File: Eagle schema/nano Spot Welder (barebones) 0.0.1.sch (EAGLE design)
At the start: 37 parts, among them Q1 BC548, Q3 BD137, T1 BTA 41 / 600V, U1 NANO, U2 DISPLAY-NOKIA-5110, U3 DS18B20, X3 ~230V, X4 Mikro trafó

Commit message: - eagle schemas
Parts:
- removed U1: NANO, Arduino-clone:NANO
- added C2, C3: 33p, rcl:C-EU025-024X044
- added C4, C5: 100n, rcl:C-EU025-024X044
- added C6: 220u, resistor:CPOL-EUE5-4
- added D2: 1N4148, diode:1N4148DO35-10
- added IC1: 7805T, linear:7805T
- added IC2: 78L33, linear:7805L
- added J1: AVR ISP CONN, SparkFun-Connectors:CONN_03X2SHROUD
- added R6: 1k, resistor:R-EU_0204/7
- added U4: 328P, SparkFun-IC-Microcontroller:ATMEGA328P_PDIP
- added Y1: 16MHz, SparkFun-Clocks:CRYSTAL-16MHZPTH-HC49US
- added ~TÁP: ~9V, con-ptr500:AK300/2
- B1: value (none) -> 1W01M
- R5: value 56kk -> 4k7
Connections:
- removed net +5V: U1.5.5V
- new net N$10: C3.2, U4.PB7(XTAL2/TOSC2), Y1.1
- new net N$11: B1.+, D2.A, R5.1
- new net N$8: C4.2, U4.AREF
- new net N$9: C2.2, U4.PB6(XTAL1/TOSC1), Y1.2
- new net RST: J1.5, R6.2, U4.PC6(/RESET)
- new net VCC1: B1.AC1, ~TÁP-2.KL
- net +3.3V: now also IC2.VO; no longer U1.3.3V
- net A0: now also U4.PC0(ADC0); no longer U1.A0
- net A1: now also U4.PC1(ADC1); no longer U1.A1
- net A2: now also U4.PC2(ADC2); no longer U1.A2
- net A3: now also U4.PC3(ADC3); no longer U1.A3
- net D10: now also U4.PB2(SS/OC1B); no longer U1.D10
- net D11: now also J1.4, U4.PB3(MOSI/OC2); no longer U1.D11
- net D12: now also J1.1, U4.PB4(MISO); no longer U1.D12
- net D13: now also J1.3, U4.PB5(SCK); no longer U1.D13
- net D2: now also U4.PD2(INT0); no longer U1.D2
- net D3: now also U4.PD3(INT1); no longer U1.D3
- net D4: now also U4.PD4(XCK/T0); no longer U1.D4
- net D5: now also U4.PD5(T1); no longer U1.D5
- net D6: now also U4.PD6(AIN0); no longer U1.D6
- net D7: now also U4.PD7(AIN1); no longer U1.D7
- net D8: now also U4.PB0(ICP); no longer U1.D8
- net D9: now also U4.PB1(OC1A); no longer U1.D9
- net GND: now also C2.1, C3.1, C4.1, C5.1, C6.-, IC1.GND, IC2.GND, J1.6, U4.GND@1, U4.GND@2; no longer U1.GND
- net N$25: no longer B1.AC1
- net N$3: now also R5.2; no longer B1.+
- net N$33: no longer R5.2
- net N$7: now also ~TÁP-1.KL; no longer R5.1
- net VCC: now also C5.2, C6.+, D2.C, IC1.VI, IC1.VO, IC2.VI, J1.2, R6.1, U4.AVCC, U4.VCC
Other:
- note added: "+"
- note added: "Arduino Nano MOT vezérlő (barebones)"
- note added: "GND"
- note added: "MISO"
- note added: "MOSI"
- note added: "RST"
- note added: "SCK"
- note removed: "Arduino Nano MOT vezérlő"
- moved on the sheet: B1, OK1, R2, R3, R5

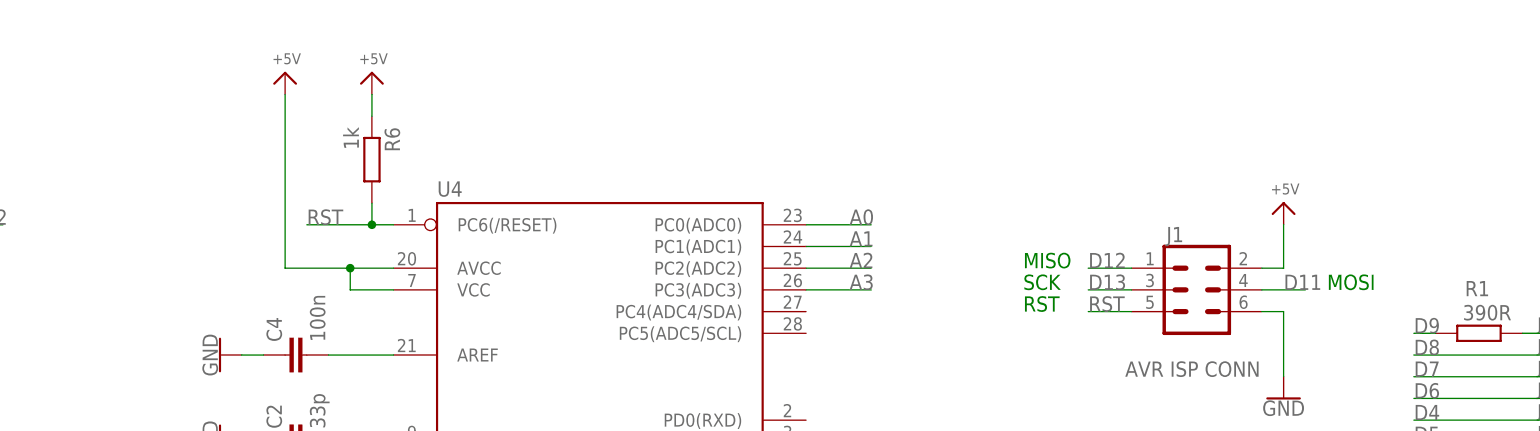
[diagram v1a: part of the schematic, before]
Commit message: - LCD szintillesztő ellenállások - LCD bias & Contrast
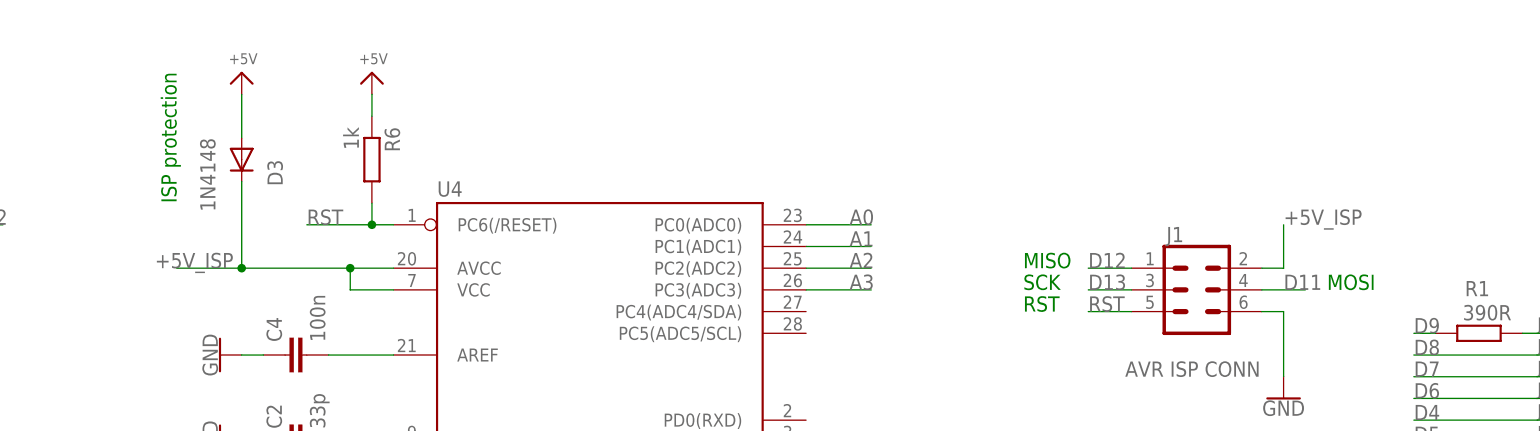
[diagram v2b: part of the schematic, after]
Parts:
- added D3: 1N4148, diode:1N4148DO35-10
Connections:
- new net +5V_ISP: D3.C, J1.2, U4.AVCC, U4.VCC
- net VCC: now also D3.A; no longer J1.2, U4.AVCC, U4.VCC
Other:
- note added: "ISP protection"
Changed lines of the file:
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@@
 <part name="GND15" library="SparkFun-PowerSymbols" library_urn="urn:adsk.eagle:library:530" deviceset="GND" device=""/>
 <part name="R6" library="resistor" library_urn="urn:adsk.eagle:library:348" deviceset="R-EU_" device="0204/7" package3d_urn="urn:adsk.eagle:package:25945/1" value="1k"/>
-<part name="P+5" library="audio amplifier example" library_urn="urn:adsk.eagle:library:970892" deviceset="VCC" device="" value="+5V"/>
 <part name="IC1" library="linear" library_urn="urn:adsk.eagle:library:262" deviceset="78*" device="T" package3d_urn="urn:adsk.eagle:package:16414/1" technology="05"/>
 <part name="IC2" library="linear" library_urn="urn:adsk.eagle:library:262" deviceset="78*" device="L" package3d_urn="urn:adsk.eagle:package:16416/2" technology="05" value="78L33"/>
 <part name="J1" library="SparkFun-Connectors" library_urn="urn:adsk.eagle:library:513" deviceset="CONN_03X2" device="SHROUD" package3d_urn="urn:adsk.eagle:package:38264/1" value="AVR ISP CONN"/>
-<part name="P+8" library="audio amplifier example" library_urn="urn:adsk.eagle:library:970892" deviceset="VCC" device="" value="+5V"/>
 <part name="GND5" library="SparkFun-PowerSymbols" library_urn="urn:adsk.eagle:library:530" deviceset="GND" device=""/>
 <part name="P+9" library="audio amplifier example" library_urn="urn:adsk.eagle:library:970892" deviceset="VCC" device="" value="+5V"/>
@@
 <part name="R5" library="resistor" library_urn="urn:adsk.eagle:library:348" deviceset="R-EU_" device="0204/7" package3d_urn="urn:adsk.eagle:package:25945/1" value="4k7"/>
 <part name="~TÁP" library="con-ptr500" library_urn="urn:adsk.eagle:library:181" deviceset="AK300/2" device="" package3d_urn="urn:adsk.eagle:package:9881/1" value="~9V"/>
+<part name="D3" library="diode" library_urn="urn:adsk.eagle:library:210" deviceset="1N4148" device="DO35-10" package3d_urn="urn:adsk.eagle:package:43344/2" value="1N4148"/>
+<part name="P+5" library="audio amplifier example" library_urn="urn:adsk.eagle:library:970892" deviceset="VCC" device="" value="+5V"/>
 </parts>
 <sheets>
@@
 <text x="25.4" y="121.92" size="1.778" layer="91">SCK</text>
 <text x="25.4" y="119.38" size="1.778" layer="91">RST</text>
+<text x="-73.66" y="132.08" size="1.778" layer="91" rot="R90">
+ISP protection </text>
 </plain>
 <instances>
@@
 <attribute name="VALUE" x="-54.102" y="140.97" size="1.778" layer="96" rot="R270"/>
 </instance>
-<instance part="P+5" gate="VCC" x="-60.96" y="147.32"/>
 <instance part="IC1" gate="A1" x="-152.4" y="12.7"/>
 <instance part="IC2" gate="A1" x="-121.92" y="12.7"/>
@@
 <attribute name="VALUE" x="37.338" y="113.538" size="1.778" layer="96" font="vector" align="top-left"/>
 </instance>
-<instance part="P+8" gate="VCC" x="55.88" y="132.08"/>
 <instance part="GND5" gate="1" x="55.88" y="109.22"/>
 <instance part="P+9" gate="VCC" x="-50.8" y="147.32"/>
@@
 <attribute name="VALUE" x="-156.21" y="72.263" size="1.778" layer="96" rot="MR180"/>
 </instance>
+<instance part="D3" gate="G$1" x="-66.04" y="137.16" smashed="yes" rot="R270">
+<attribute name="NAME" x="-63.0174" y="137.16" size="1.778" layer="95" rot="R270"/>
+<attribute name="VALUE" x="-70.8914" y="139.7" size="1.778" layer="96" rot="R270"/>
+</instance>
+<instance part="P+5" gate="VCC" x="-66.04" y="147.32"/>
 </instances>
 <busses>
@@
 </segment>
 <segment>
-<pinref part="J1" gate="G$1" pin="2"/>
-<wire x1="53.34" y1="124.46" x2="55.88" y2="124.46" width="0.1524" layer="91"/>
-<pinref part="P+8" gate="VCC" pin="VCC"/>
-<wire x1="55.88" y1="124.46" x2="55.88" y2="129.54" width="0.1524" layer="91"/>
-</segment>
-<segment>
-<pinref part="U4" gate="G$1" pin="VCC"/>
-<wire x1="-53.34" y1="121.92" x2="-48.26" y2="121.92" width="0.1524" layer="91"/>
-<pinref part="U4" gate="G$1" pin="AVCC"/>
-<wire x1="-48.26" y1="124.46" x2="-53.34" y2="124.46" width="0.1524" layer="91"/>
-<wire x1="-53.34" y1="124.46" x2="-53.34" y2="121.92" width="0.1524" layer="91"/>
-<wire x1="-53.34" y1="124.46" x2="-60.96" y2="124.46" width="0.1524" layer="91"/>
-<junction x="-53.34" y="124.46"/>
-<pinref part="P+5" gate="VCC" pin="VCC"/>
-<wire x1="-60.96" y1="124.46" x2="-60.96" y2="144.78" width="0.1524" layer="91"/>
-</segment>
-<segment>
 <pinref part="R6" gate="G$1" pin="1"/>
 <pinref part="P+9" gate="VCC" pin="VCC"/>
@@
 <wire x1="-165.1" y1="12.7" x2="-165.1" y2="27.94" width="0.1524" layer="91"/>
 </segment>
+<segment>
+<pinref part="D3" gate="G$1" pin="A"/>
+<pinref part="P+5" gate="VCC" pin="VCC"/>
+<wire x1="-66.04" y1="139.7" x2="-66.04" y2="144.78" width="0.1524" layer="91"/>
+</segment>
 </net>
 <net name="A2" class="0">
@@
 </segment>
 </net>
+<net name="+5V_ISP" class="0">
+<segment>
+<pinref part="U4" gate="G$1" pin="VCC"/>
+<wire x1="-53.34" y1="121.92" x2="-48.26" y2="121.92" width="0.1524" layer="91"/>
+<pinref part="U4" gate="G$1" pin="AVCC"/>
+<wire x1="-48.26" y1="124.46" x2="-53.34" y2="124.46" width="0.1524" layer="91"/>
+<wire x1="-53.34" y1="124.46" x2="-53.34" y2="121.92" width="0.1524" layer="91"/>
+<wire x1="-53.34" y1="124.46" x2="-66.04" y2="124.46" width="0.1524" layer="91"/>
+<junction x="-53.34" y="124.46"/>
+<pinref part="D3" gate="G$1" pin="C"/>
+<wire x1="-66.04" y1="124.46" x2="-66.04" y2="134.62" width="0.1524" layer="91"/>
+<wire x1="-66.04" y1="124.46" x2="-73.66" y2="124.46" width="0.1524" layer="91"/>
+<junction x="-66.04" y="124.46"/>
+<label x="-76.2" y="124.46" size="1.778" layer="95"/>
+</segment>
+<segment>
+<pinref part="J1" gate="G$1" pin="2"/>
+<wire x1="53.34" y1="124.46" x2="55.88" y2="124.46" width="0.1524" layer="91"/>
+<wire x1="55.88" y1="124.46" x2="55.88" y2="129.54" width="0.1524" layer="91"/>
+<label x="55.88" y="129.54" size="1.778" layer="95"/>
+</segment>
+</net>
 </nets>
 </sheet>
@@
 </drawing>
 <compatibility>
+<note version="6.3" minversion="6.2.2" severity="warning">
+Since Version 6.2.2 text objects can contain more than one line,
+which will not be processed correctly with this version.
+</note>
 <note version="8.2" severity="warning">
 Since Version 8.2, EAGLE supports online libraries. The ids

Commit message: - rajzok
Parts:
- removed C4: 100n, rcl:C-EU025-024X044
- removed D3: 1N4148, diode:1N4148DO35-10
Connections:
- removed net N$8: C4.2, U4.AREF
- net +5V_ISP: now also U4.AREF; no longer D3.C
- net GND: no longer C4.1
- net VCC: no longer D3.A
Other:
- note removed: "ISP protection"
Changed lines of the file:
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@@
 <part name="GND13" library="SparkFun-PowerSymbols" library_urn="urn:adsk.eagle:library:530" deviceset="GND" device=""/>
 <part name="GND14" library="SparkFun-PowerSymbols" library_urn="urn:adsk.eagle:library:530" deviceset="GND" device=""/>
-<part name="C4" library="rcl" library_urn="urn:adsk.eagle:library:334" deviceset="C-EU" device="025-024X044" package3d_urn="urn:adsk.eagle:package:23630/1" value="100n"/>
-<part name="GND15" library="SparkFun-PowerSymbols" library_urn="urn:adsk.eagle:library:530" deviceset="GND" device=""/>
 <part name="R6" library="resistor" library_urn="urn:adsk.eagle:library:348" deviceset="R-EU_" device="0204/7" package3d_urn="urn:adsk.eagle:package:25945/1" value="1k"/>
 <part name="IC1" library="linear" library_urn="urn:adsk.eagle:library:262" deviceset="78*" device="T" package3d_urn="urn:adsk.eagle:package:16414/1" technology="05"/>
@@
 <part name="R5" library="resistor" library_urn="urn:adsk.eagle:library:348" deviceset="R-EU_" device="0204/7" package3d_urn="urn:adsk.eagle:package:25945/1" value="4k7"/>
 <part name="~TÁP" library="con-ptr500" library_urn="urn:adsk.eagle:library:181" deviceset="AK300/2" device="" package3d_urn="urn:adsk.eagle:package:9881/1" value="~9V"/>
-<part name="D3" library="diode" library_urn="urn:adsk.eagle:library:210" deviceset="1N4148" device="DO35-10" package3d_urn="urn:adsk.eagle:package:43344/2" value="1N4148"/>
 <part name="P+5" library="audio amplifier example" library_urn="urn:adsk.eagle:library:970892" deviceset="VCC" device="" value="+5V"/>
 </parts>
@@
 <text x="25.4" y="121.92" size="1.778" layer="91">SCK</text>
 <text x="25.4" y="119.38" size="1.778" layer="91">RST</text>
-<text x="-73.66" y="132.08" size="1.778" layer="91" rot="R90">
-ISP protection </text>
 </plain>
 <instances>
@@
 <instance part="GND13" gate="1" x="-68.58" y="99.06" rot="R270"/>
 <instance part="GND14" gate="1" x="-53.34" y="68.58"/>
-<instance part="C4" gate="G$1" x="-60.96" y="114.3" rot="R90"/>
-<instance part="GND15" gate="1" x="-68.58" y="114.3" rot="R270"/>
 <instance part="R6" gate="G$1" x="-50.8" y="137.16" smashed="yes" rot="R270">
 <attribute name="NAME" x="-49.3014" y="140.97" size="1.778" layer="95" rot="R270"/>
@@
 <attribute name="NAME" x="-161.29" y="67.691" size="1.778" layer="95" rot="MR0"/>
 <attribute name="VALUE" x="-156.21" y="72.263" size="1.778" layer="96" rot="MR180"/>
-</instance>
-<instance part="D3" gate="G$1" x="-66.04" y="137.16" smashed="yes" rot="R270">
-<attribute name="NAME" x="-63.0174" y="137.16" size="1.778" layer="95" rot="R270"/>
-<attribute name="VALUE" x="-70.8914" y="139.7" size="1.778" layer="96" rot="R270"/>
 </instance>
 <instance part="P+5" gate="VCC" x="-66.04" y="147.32"/>
@@
 <wire x1="-53.34" y1="73.66" x2="-53.34" y2="71.12" width="0.1524" layer="91"/>
 <junction x="-53.34" y="73.66"/>
-</segment>
-<segment>
-<pinref part="GND15" gate="1" pin="GND"/>
-<pinref part="C4" gate="G$1" pin="1"/>
-<wire x1="-66.04" y1="114.3" x2="-63.5" y2="114.3" width="0.1524" layer="91"/>
 </segment>
 <segment>
@@
 <wire x1="-165.1" y1="12.7" x2="-165.1" y2="27.94" width="0.1524" layer="91"/>
 </segment>
-<segment>
-<pinref part="D3" gate="G$1" pin="A"/>
-<pinref part="P+5" gate="VCC" pin="VCC"/>
-<wire x1="-66.04" y1="139.7" x2="-66.04" y2="144.78" width="0.1524" layer="91"/>
-</segment>
 </net>
 <net name="A2" class="0">
@@
 <wire x1="-149.86" y1="63.5" x2="-154.94" y2="63.5" width="0.1524" layer="91"/>
 <wire x1="-149.86" y1="60.96" x2="-149.86" y2="63.5" width="0.1524" layer="91"/>
-</segment>
-</net>
-<net name="N$8" class="0">
-<segment>
-<pinref part="U4" gate="G$1" pin="AREF"/>
-<pinref part="C4" gate="G$1" pin="2"/>
-<wire x1="-55.88" y1="114.3" x2="-48.26" y2="114.3" width="0.1524" layer="91"/>
 </segment>
 </net>
@@
 <net name="+5V_ISP" class="0">
 <segment>
+<pinref part="J1" gate="G$1" pin="2"/>
+<wire x1="53.34" y1="124.46" x2="55.88" y2="124.46" width="0.1524" layer="91"/>
+<wire x1="55.88" y1="124.46" x2="55.88" y2="129.54" width="0.1524" layer="91"/>
+<label x="55.88" y="129.54" size="1.778" layer="95"/>
+</segment>
+<segment>
+<pinref part="P+5" gate="VCC" pin="VCC"/>
 <pinref part="U4" gate="G$1" pin="VCC"/>
 <wire x1="-53.34" y1="121.92" x2="-48.26" y2="121.92" width="0.1524" layer="91"/>
@@
 <wire x1="-53.34" y1="124.46" x2="-66.04" y2="124.46" width="0.1524" layer="91"/>
 <junction x="-53.34" y="124.46"/>
-<pinref part="D3" gate="G$1" pin="C"/>
-<wire x1="-66.04" y1="124.46" x2="-66.04" y2="134.62" width="0.1524" layer="91"/>
+<wire x1="-66.04" y1="124.46" x2="-66.04" y2="144.78" width="0.1524" layer="91"/>
 <wire x1="-66.04" y1="124.46" x2="-73.66" y2="124.46" width="0.1524" layer="91"/>
 <junction x="-66.04" y="124.46"/>
 <label x="-76.2" y="124.46" size="1.778" layer="95"/>
-</segment>
-<segment>
-<pinref part="J1" gate="G$1" pin="2"/>
-<wire x1="53.34" y1="124.46" x2="55.88" y2="124.46" width="0.1524" layer="91"/>
-<wire x1="55.88" y1="124.46" x2="55.88" y2="129.54" width="0.1524" layer="91"/>
-<label x="55.88" y="129.54" size="1.778" layer="95"/>
+<wire x1="-53.34" y1="121.92" x2="-53.34" y2="114.3" width="0.1524" layer="91"/>
+<junction x="-53.34" y="121.92"/>
+<pinref part="U4" gate="G$1" pin="AREF"/>
+<wire x1="-53.34" y1="114.3" x2="-48.26" y2="114.3" width="0.1524" layer="91"/>
 </segment>
 </net>
@@
 </drawing>
 <compatibility>
-<note version="6.3" minversion="6.2.2" severity="warning">
-Since Version 6.2.2 text objects can contain more than one line,
-which will not be processed correctly with this version.
-</note>
 <note version="8.2" severity="warning">
 Since Version 8.2, EAGLE supports online libraries. The ids
